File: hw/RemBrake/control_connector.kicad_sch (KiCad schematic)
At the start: 9 parts, among them J4 Conn_01x08_MountingPin, J5 Conn_01x04_MountingPin, J6 Conn_01x03_MountingPin

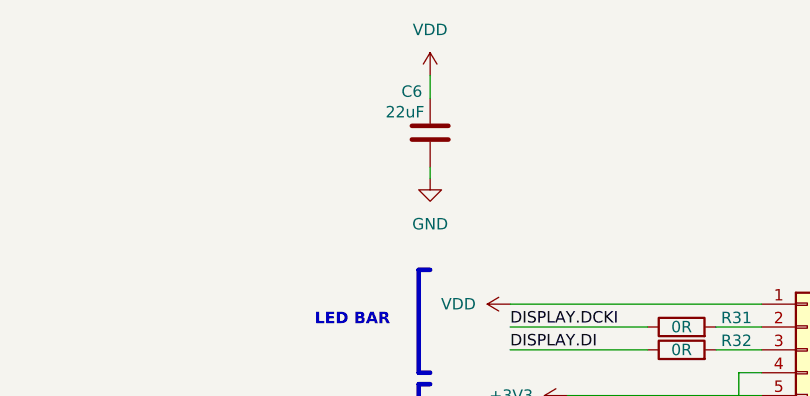
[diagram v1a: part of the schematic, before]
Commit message: updated BOM list and reduced number of different capacitors and resistors
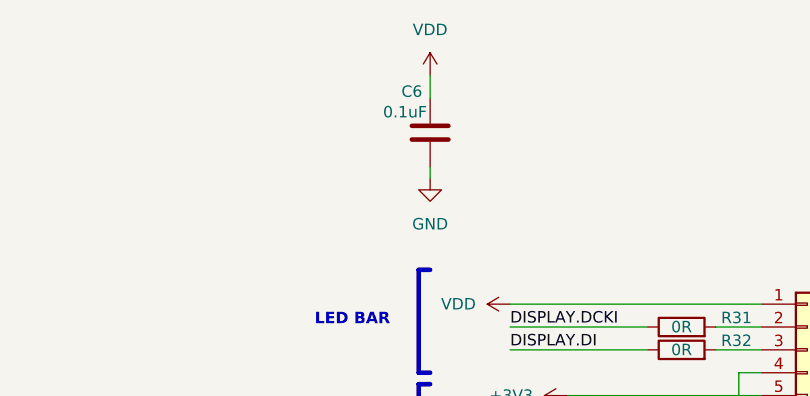
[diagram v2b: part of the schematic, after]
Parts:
- C6: value 22uF -> 0.1uF
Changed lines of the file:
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@@
 			)
 		)
-		(property "Value" "22uF"
+		(property "Value" "0.1uF"
 			(at 172.466 37.084 0)
 			(effects
